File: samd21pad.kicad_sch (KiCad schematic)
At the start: 26 parts, among them J1 USB_C_Receptacle_USB2.0, J2 Conn_ARM_SWD_TagConnect_TC203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, SW1 SW_Push, SW10 SKQGAKE020, SW2 SW_Push, SW3 SW_Push, SW4 SW_Push, SW5 SW_Push, SW6 SW_Push, SW7 SW_Push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

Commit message: General routing clean ups, silk tweaks, etc.
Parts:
- renumbered SW4 to SW2, SW2 to SW4
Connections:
- net SW2: now also SW2.1, U1.17 (PA16); no longer SW4.1, U1.14 (PA11)
- net SW3: now also U1.18 (PA17); no longer U1.15 (PA14)
- net SW4: now also SW4.1, U1.14 (PA11); no longer SW5.1, U1.17 (PA16)
- net SW5: now also SW5.1, U1.20 (PA19); no longer SW2.1, U1.18 (PA17)
- net SW6: now also U1.22 (PA23); no longer U1.19 (PA18)
- net SW7: now also U1.15 (PA14); no longer U1.20 (PA19)
- net SW8: now also U1.19 (PA18); no longer U1.21 (PA22)
- net SW9: now also U1.21 (PA22); no longer U1.22 (PA23)
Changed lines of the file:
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@@
     (stroke (width 0) (type default))
   )
-  (global_label "SW7" (shape input) (at 224.79 96.52 180) (fields_autoplaced)
+  (global_label "SW5" (shape input) (at 224.79 96.52 180) (fields_autoplaced)
     (effects (font (size 1.27 1.27)) (justify right))
     (property "Intersheetrefs" "${INTERSHEET_REFS}" (at 218.0138 96.52 0)
@@
     )
   )
-  (global_label "SW9" (shape input) (at 224.79 106.68 180) (fields_autoplaced)
+  (global_label "SW6" (shape input) (at 224.79 106.68 180) (fields_autoplaced)
     (effects (font (size 1.27 1.27)) (justify right))
     (property "Intersheetrefs" "${INTERSHEET_REFS}" (at 218.0138 106.68 0)
@@
     )
   )
-  (global_label "SW8" (shape input) (at 224.79 104.14 180) (fields_autoplaced)
+  (global_label "SW9" (shape input) (at 224.79 104.14 180) (fields_autoplaced)
     (effects (font (size 1.27 1.27)) (justify right))
     (property "Intersheetrefs" "${INTERSHEET_REFS}" (at 218.0138 104.14 0)
@@
     )
   )
-  (global_label "SW6" (shape input) (at 224.79 93.98 180) (fields_autoplaced)
+  (global_label "SW8" (shape input) (at 224.79 93.98 180) (fields_autoplaced)
     (effects (font (size 1.27 1.27)) (justify right))
     (property "Intersheetrefs" "${INTERSHEET_REFS}" (at 218.0138 93.98 0)
@@
     )
   )
-  (global_label "SW5" (shape input) (at 111.76 96.52 180) (fields_autoplaced)
+  (global_label "SW2" (shape input) (at 111.76 96.52 180) (fields_autoplaced)
     (effects (font (size 1.27 1.27)) (justify right))
     (property "Intersheetrefs" "${INTERSHEET_REFS}" (at 104.9838 96.52 0)
@@
     )
   )
-  (global_label "SW4" (shape input) (at 129.54 96.52 180) (fields_autoplaced)
+  (global_label "SW5" (shape input) (at 129.54 96.52 180) (fields_autoplaced)
     (effects (font (size 1.27 1.27)) (justify right))
     (property "Intersheetrefs" "${INTERSHEET_REFS}" (at 122.7638 96.52 0)
@@
     )
   )
-  (global_label "SW5" (shape input) (at 224.79 91.44 180) (fields_autoplaced)
+  (global_label "SW3" (shape input) (at 224.79 91.44 180) (fields_autoplaced)
     (effects (font (size 1.27 1.27)) (justify right))
     (property "Intersheetrefs" "${INTERSHEET_REFS}" (at 218.0138 91.44 0)
@@
     )
   )
-  (global_label "SW2" (shape input) (at 129.54 83.82 180) (fields_autoplaced)
+  (global_label "SW4" (shape input) (at 129.54 83.82 180) (fields_autoplaced)
     (effects (font (size 1.27 1.27)) (justify right))
     (property "Intersheetrefs" "${INTERSHEET_REFS}" (at 122.7638 83.82 0)
@@
     )
   )
-  (global_label "SW3" (shape input) (at 224.79 83.82 180) (fields_autoplaced)
+  (global_label "SW7" (shape input) (at 224.79 83.82 180) (fields_autoplaced)
     (effects (font (size 1.27 1.27)) (justify right))
     (property "Intersheetrefs" "${INTERSHEET_REFS}" (at 218.0138 83.82 0)
@@
     )
   )
-  (global_label "SW2" (shape input) (at 224.79 76.2 180) (fields_autoplaced)
+  (global_label "SW4" (shape input) (at 224.79 76.2 180) (fields_autoplaced)
     (effects (font (size 1.27 1.27)) (justify right))
     (property "Intersheetrefs" "${INTERSHEET_REFS}" (at 218.0138 76.2 0)
@@
     )
   )
-  (global_label "SW4" (shape input) (at 224.79 88.9 180) (fields_autoplaced)
+  (global_label "SW2" (shape input) (at 224.79 88.9 180) (fields_autoplaced)
     (effects (font (size 1.27 1.27)) (justify right))
     (property "Intersheetrefs" "${INTERSHEET_REFS}" (at 218.0138 88.9 0)
@@
   (symbol (lib_id "Switch:SW_Push") (at 134.62 83.82 0) (unit 1)
     (in_bom yes) (on_board yes) (dnp no) (fields_autoplaced)
-    (property "Reference" "SW2" (at 134.62 76.2 0)
+    (property "Reference" "SW4" (at 134.62 76.2 0)
       (effects (font (size 1.27 1.27)))
     )
@@
       (project "samd21pad"
         (path "/eb5ab6b4-064a-4956-9e6e-ad6326fd260d"
-          (reference "SW2") (unit 1)
+          (reference "SW4") (unit 1)
         )
       )
@@
   (symbol (lib_id "Switch:SW_Push") (at 116.84 96.52 0) (unit 1)
     (in_bom yes) (on_board yes) (dnp no) (fields_autoplaced)
-    (property "Reference" "SW4" (at 116.84 88.9 0)
+    (property "Reference" "SW2" (at 116.84 88.9 0)
       (effects (font (size 1.27 1.27)))
     )
@@
       (project "samd21pad"
         (path "/eb5ab6b4-064a-4956-9e6e-ad6326fd260d"
-          (reference "SW4") (unit 1)
-        )
-      )
+          (reference "SW2") (unit 1)
+        )
+      )

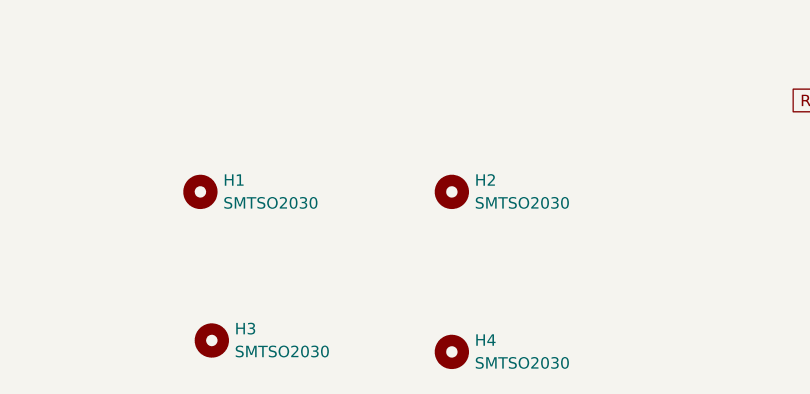
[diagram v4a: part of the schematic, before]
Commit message: Fix the solder nut part/JLC number.
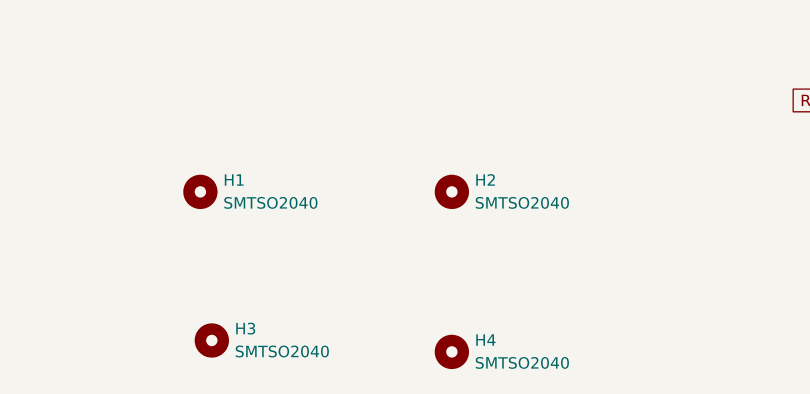
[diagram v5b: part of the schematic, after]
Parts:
- H1, H2, H3, H4: value SMTSO2030 -> SMTSO2040; LCSC Part Number C2928170 -> C2916349
- U2: LCSC Part Number C51118 -> C3021085
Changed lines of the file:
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@@
       (effects (font (size 1.27 1.27)) hide)
     )
-    (property "LCSC Part Number" "C51118" (at 102.87 39.37 0)
+    (property "LCSC Part Number" "C3021085" (at 102.87 39.37 0)
       (effects (font (size 1.27 1.27)) hide)
     )
@@
       (effects (font (size 1.27 1.27)) (justify left))
     )
-    (property "Value" "SMTSO2030" (at 73.66 163.83 0)
+    (property "Value" "SMTSO2040" (at 73.66 163.83 0)
       (effects (font (size 1.27 1.27)) (justify left))
     )
@@
       (effects (font (size 1.27 1.27)) hide)
     )
-    (property "LCSC Part Number" "C2928170" (at 71.12 162.56 0)
+    (property "LCSC Part Number" "C2916349 " (at 71.12 162.56 0)
       (effects (font (size 1.27 1.27)) hide)
     )
@@
       (effects (font (size 1.27 1.27)) (justify left))
     )
-    (property "Value" "SMTSO2030" (at 101.6 163.83 0)
+    (property "Value" "SMTSO2040" (at 101.6 163.83 0)
       (effects (font (size 1.27 1.27)) (justify left))
     )
@@
       (effects (font (size 1.27 1.27)) hide)
     )
-    (property "LCSC Part Number" "C2928170" (at 99.06 162.56 0)
+    (property "LCSC Part Number" "C2916349" (at 99.06 162.56 0)
       (effects (font (size 1.27 1.27)) hide)
     )
@@
       (effects (font (size 1.27 1.27)) (justify left))
     )
-    (property "Value" "SMTSO2030" (at 101.6 181.61 0)
+    (property "Value" "SMTSO2040" (at 101.6 181.61 0)
       (effects (font (size 1.27 1.27)) (justify left))
     )
@@
       (effects (font (size 1.27 1.27)) hide)
     )
-    (property "LCSC Part Number" "C2928170" (at 99.06 180.34 0)
+    (property "LCSC Part Number" "C2916349" (at 99.06 180.34 0)
       (effects (font (size 1.27 1.27)) hide)
     )
@@
       (effects (font (size 1.27 1.27)) (justify left))
     )
-    (property "Value" "SMTSO2030" (at 74.93 180.34 0)
+    (property "Value" "SMTSO2040" (at 74.93 180.34 0)
       (effects (font (size 1.27 1.27)) (justify left))
     )
@@
       (effects (font (size 1.27 1.27)) hide)
     )
-    (property "LCSC Part Number" "C2928170" (at 72.39 179.07 0)
-      (effects (font (size 1.27 1.27)) hide)
-    )
+    (property "LCSC Part Number" "C2916349" (at 72.39 179.07 0)
+      (effects (font (size 1.27 1.27)) hide)
+    )

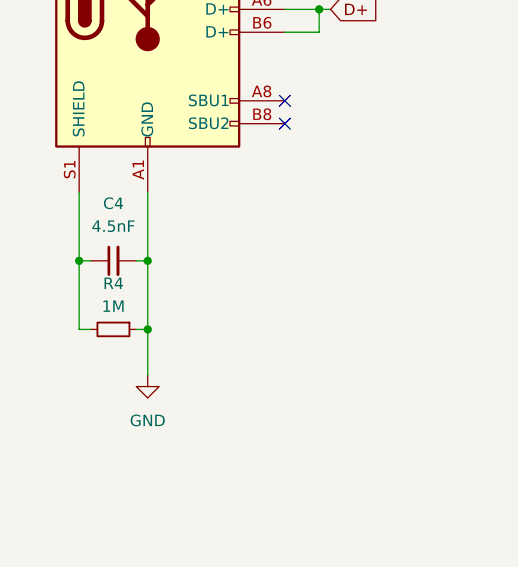
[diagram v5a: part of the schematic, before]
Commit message: Tweaks for USB shield handling, nuke meetup silk.
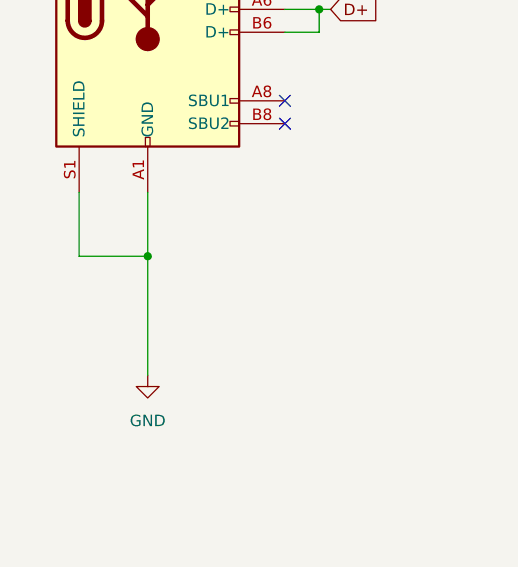
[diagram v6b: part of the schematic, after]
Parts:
- removed C4: 4.5nF, Capacitor_SMD:C_0805_2012Metric, symbol Device:C_Small
- removed R4: 1M, Resistor_SMD:R_0805_2012Metric, symbol Device:R_Small
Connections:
- net GND: now also J1.S1 (SHIELD)
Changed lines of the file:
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@@
   (junction (at 92.71 36.83) (diameter 0) (color 0 0 0 0)
   )
-  (junction (at 49.53 128.27) (diameter 0) (color 0 0 0 0)
-  )
   (junction (at 157.48 109.22) (diameter 0) (color 0 0 0 0)
   )
@@
   (junction (at 68.58 92.71) (diameter 0) (color 0 0 0 0)
   )
-  (junction (at 49.53 120.65) (diameter 0) (color 0 0 0 0)
-  )
-  (junction (at 41.91 120.65) (diameter 0) (color 0 0 0 0)
-  )
   (junction (at 85.09 82.55) (diameter 0) (color 0 0 0 0)
   )
@@
   )
   (junction (at 102.87 49.53) (diameter 0) (color 0 0 0 0)
+  )
+  (junction (at 49.53 120.142) (diameter 0) (color 0 0 0 0)
   )
   (no_connect (at 64.77 102.87))
@@
     (stroke (width 0) (type default))
   )
-  (wire (pts (xy 49.53 120.65) (xy 49.53 128.27))
+  (wire (pts (xy 49.53 113.03) (xy 49.53 120.142))
     (stroke (width 0) (type default))
   )
@@
     (stroke (width 0) (type default))
   )
-  (wire (pts (xy 41.91 128.27) (xy 43.18 128.27))
+  (wire (pts (xy 49.53 120.142) (xy 49.53 133.35))
     (stroke (width 0) (type default))
   )
@@
     (stroke (width 0) (type default))
   )
-  (wire (pts (xy 48.26 120.65) (xy 49.53 120.65))
-    (stroke (width 0) (type default))
-  )
   (wire (pts (xy 64.77 87.63) (xy 68.58 87.63))
     (stroke (width 0) (type default))
@@
     (stroke (width 0) (type default))
   )
-  (wire (pts (xy 41.91 113.03) (xy 41.91 120.65))
+  (wire (pts (xy 41.91 113.03) (xy 41.91 120.142))
     (stroke (width 0) (type default))
   )
@@
     (stroke (width 0) (type default))
   )
-  (wire (pts (xy 41.91 120.65) (xy 43.18 120.65))
-    (stroke (width 0) (type default))
-  )
   (wire (pts (xy 215.9 124.46) (xy 217.17 124.46))
     (stroke (width 0) (type default))
@@
     (stroke (width 0) (type default))
   )
-  (wire (pts (xy 48.26 128.27) (xy 49.53 128.27))
-    (stroke (width 0) (type default))
-  )
   (wire (pts (xy 250.19 40.64) (xy 250.19 21.59))
     (stroke (width 0) (type default))
@@
     (stroke (width 0) (type default))
   )
-  (wire (pts (xy 41.91 120.65) (xy 41.91 128.27))
-    (stroke (width 0) (type default))
-  )
-  (wire (pts (xy 49.53 128.27) (xy 49.53 133.35))
+  (wire (pts (xy 41.91 120.142) (xy 49.53 120.142))
     (stroke (width 0) (type default))
   )
@@
   )
   (wire (pts (xy 234.95 31.75) (xy 234.95 40.64))
-    (stroke (width 0) (type default))
-  )
-  (wire (pts (xy 49.53 113.03) (xy 49.53 120.65))
     (stroke (width 0) (type default))
   )
@@
         (path "/eb5ab6b4-064a-4956-9e6e-ad6326fd260d"
           (reference "#PWR017") (unit 1)
-        )
-      )
-    )
-  )
-  (symbol (lib_id "Device:C_Small") (at 45.72 120.65 90) (unit 1)
-    (in_bom yes) (on_board yes) (dnp no) (fields_autoplaced)
-    (property "Reference" "C4" (at 45.7263 114.3 90)
-      (effects (font (size 1.27 1.27)))
-    )
-    (property "Value" "4.5nF" (at 45.7263 116.84 90)
-      (effects (font (size 1.27 1.27)))
-    )
-    (property "Footprint" "Capacitor_SMD:C_0805_2012Metric" (at 45.72 120.65 0)
-      (effects (font (size 1.27 1.27)) hide)
-    )
-    (property "Datasheet" "~" (at 45.72 120.65 0)
-      (effects (font (size 1.27 1.27)) hide)
-    )
-    (property "LCSC Part Number" "C129659" (at 45.72 120.65 0)
-      (effects (font (size 1.27 1.27)) hide)
-    )
-    (property "MPN" "" (at 45.72 120.65 0)
-      (effects (font (size 1.27 1.27)) hide)
-    )
-    (pin "1")
-    (pin "2")
-    (instances
-      (project "samd21pad"
-        (path "/eb5ab6b4-064a-4956-9e6e-ad6326fd260d"
-          (reference "C4") (unit 1)
         )
       )
@@
         )
       )
-    )
-  )
-  (symbol (lib_id "Device:R_Small") (at 45.72 128.27 270) (unit 1)
-    (in_bom yes) (on_board yes) (dnp no) (fields_autoplaced)
-    (property "Reference" "R4" (at 45.72 123.19 90)
-      (effects (font (size 1.27 1.27)))
-    )
-    (property "Value" "1M" (at 45.72 125.73 90)
-      (effects (font (size 1.27 1.27)))
-    )
-    (property "Footprint" "Resistor_SMD:R_0805_2012Metric" (at 45.72 128.27 0)
-      (effects (font (size 1.27 1.27)) hide)
-    )
-    (property "Datasheet" "~" (at 45.72 128.27 0)
-      (effects (font (size 1.27 1.27)) hide)
-    )
-    (property "LCSC Part Number" "" (at 45.72 128.27 0)
-      (effects (font (size 1.27 1.27)) hide)
-    )
-    (property "MPN" "" (at 45.72 128.27 0)
-      (effects (font (size 1.27 1.27)) hide)
-    )
-    (pin "1")
-    (pin "2")
-    (instances
-      (project "samd21pad"
-        (path "/eb5ab6b4-064a-4956-9e6e-ad6326fd260d"
-          (reference "R4") (unit 1)
-        )
-      )

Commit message: JLC KiBot fixes.
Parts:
- H1: LCSC Part Number C2916349 -> C2916349
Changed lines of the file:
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@@
       (effects (font (size 1.27 1.27)) hide)
     )
-    (property "LCSC Part Number" "C2916349 " (at 71.12 162.56 0)
+    (property "LCSC Part Number" "C2916349" (at 71.12 162.56 0)
       (effects (font (size 1.27 1.27)) hide)
     )
